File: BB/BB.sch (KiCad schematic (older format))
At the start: 14 parts, among them SW0 SW_Push, U1 AT90USB1286-AU, Y0 16Mhz

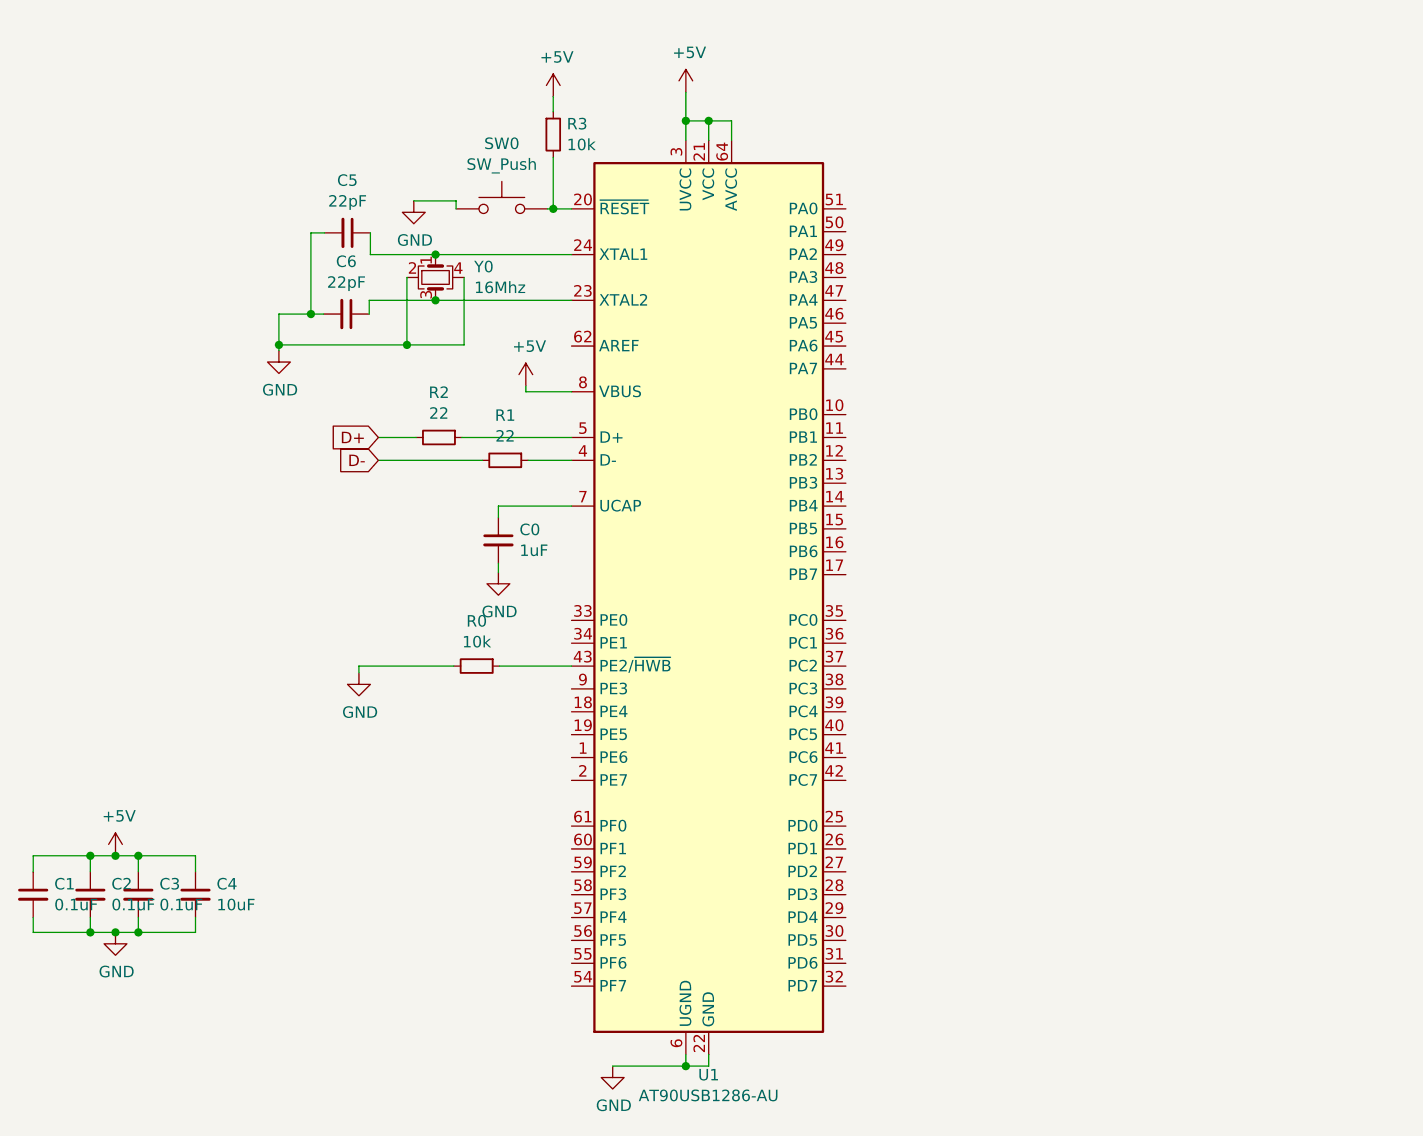
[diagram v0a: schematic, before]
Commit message: USB Molex
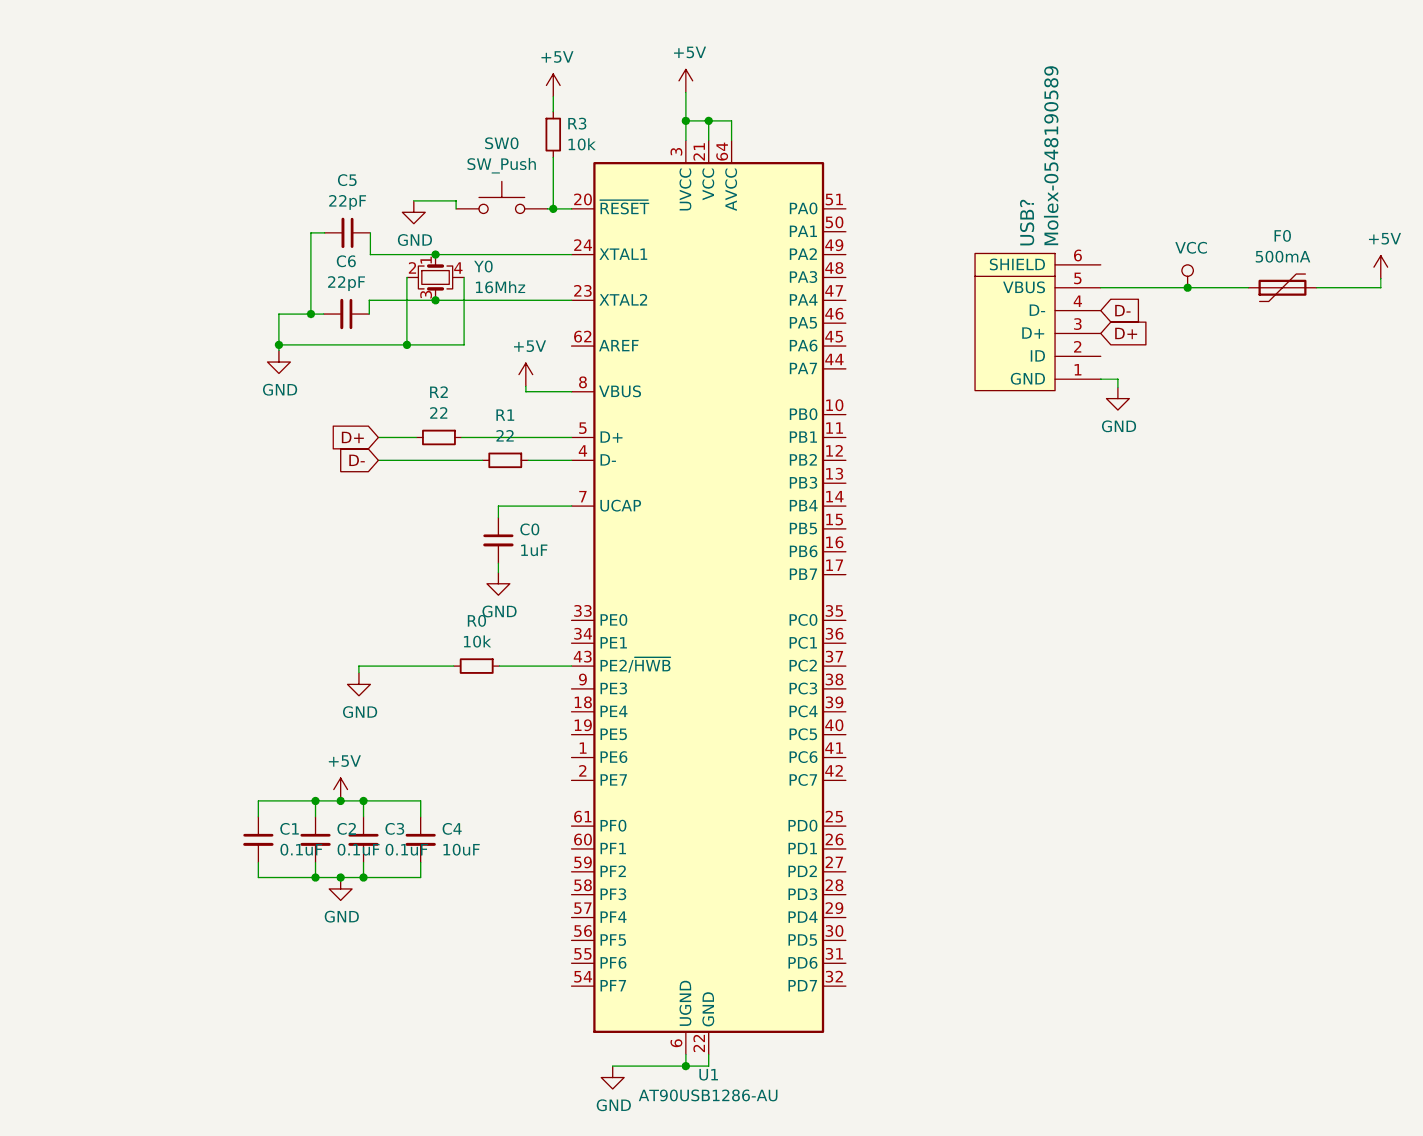
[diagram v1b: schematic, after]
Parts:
- added F0: 500mA, symbol Device:Polyfuse
- added USB?: Molex-0548190589, symbol random-keyboard-parts:Molex-0548190589
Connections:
- net +5V: now also F0.2
- net D+: now also USB?.3 (D+)
- net D-: now also USB?.4 (D-)
- net GND: now also USB?.1 (GND)
- new net VCC: F0.1, USB?.5 (VBUS)
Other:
- moved on the sheet: C1, C2, C3, C4
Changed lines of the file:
@@
 L Device:C_Small C2
 U 1 1 5CAFF9B8
-P 3100 4305
-F 0 "C2" H 3192 4351 50  0000 L CNN
-F 1 "0.1uF" H 3192 4260 50  0000 L CNN
-F 2 "" H 3100 4305 50  0001 C CNN
-F 3 "~" H 3100 4305 50  0001 C CNN
-	1    3100 4305
+P 4085 4065
+F 0 "C2" H 4177 4111 50  0000 L CNN
+F 1 "0.1uF" H 4177 4020 50  0000 L CNN
+F 2 "" H 4085 4065 50  0001 C CNN
+F 3 "~" H 4085 4065 50  0001 C CNN
+	1    4085 4065
 	1    0    0    -1
 $EndComp
@@
 L Device:C_Small C4
 U 1 1 5CB01275
-P 3560 4305
-F 0 "C4" H 3652 4351 50  0000 L CNN
-F 1 "10uF" H 3652 4260 50  0000 L CNN
-F 2 "" H 3560 4305 50  0001 C CNN
-F 3 "~" H 3560 4305 50  0001 C CNN
-	1    3560 4305
+P 4545 4065
+F 0 "C4" H 4637 4111 50  0000 L CNN
+F 1 "10uF" H 4637 4020 50  0000 L CNN
+F 2 "" H 4545 4065 50  0001 C CNN
+F 3 "~" H 4545 4065 50  0001 C CNN
+	1    4545 4065
 	1    0    0    -1
 $EndComp
@@
 L power:+5V #PWR?
 U 1 1 5CB01622
-P 3210 4135
-F 0 "#PWR?" H 3210 3985 50  0001 C CNN
-F 1 "+5V" H 3225 4308 50  0000 C CNN
-F 2 "" H 3210 4135 50  0001 C CNN
-F 3 "" H 3210 4135 50  0001 C CNN
-	1    3210 4135
+P 4195 3895
+F 0 "#PWR?" H 4195 3745 50  0001 C CNN
+F 1 "+5V" H 4210 4068 50  0000 C CNN
+F 2 "" H 4195 3895 50  0001 C CNN
+F 3 "" H 4195 3895 50  0001 C CNN
+	1    4195 3895
 	1    0    0    -1
 $EndComp
@@
 L power:GND #PWR?
 U 1 1 5CB02159
-P 3210 4470
-F 0 "#PWR?" H 3210 4220 50  0001 C CNN
-F 1 "GND" H 3215 4297 50  0000 C CNN
-F 2 "" H 3210 4470 50  0001 C CNN
-F 3 "" H 3210 4470 50  0001 C CNN
-	1    3210 4470
-	1    0    0    -1
-$EndComp
-Wire Wire Line
-	2850 4405 2850 4470
-Wire Wire Line
-	2850 4470 3100 4470
-Wire Wire Line
-	3210 4470 3310 4470
-Wire Wire Line
-	3560 4470 3560 4405
-Connection ~ 3210 4470
-Connection ~ 3310 4470
-Wire Wire Line
-	3310 4470 3560 4470
-Wire Wire Line
-	3100 4405 3100 4470
-Connection ~ 3100 4470
-Wire Wire Line
-	3100 4470 3210 4470
-Connection ~ 3210 4135
-Wire Wire Line
-	3310 4405 3310 4470
+P 4195 4230
+F 0 "#PWR?" H 4195 3980 50  0001 C CNN
+F 1 "GND" H 4200 4057 50  0000 C CNN
+F 2 "" H 4195 4230 50  0001 C CNN
+F 3 "" H 4195 4230 50  0001 C CNN
+	1    4195 4230
+	1    0    0    -1
+$EndComp
+Wire Wire Line
+	3835 4165 3835 4230
+Wire Wire Line
+	3835 4230 4085 4230
+Wire Wire Line
+	4195 4230 4295 4230
+Wire Wire Line
+	4545 4230 4545 4165
+Connection ~ 4195 4230
+Connection ~ 4295 4230
+Wire Wire Line
+	4295 4230 4545 4230
+Wire Wire Line
+	4085 4165 4085 4230
+Connection ~ 4085 4230
+Wire Wire Line
+	4085 4230 4195 4230
+Connection ~ 4195 3895
+Wire Wire Line
+	4295 4165 4295 4230
 $Comp
 L Device:C_Small C3
 U 1 1 5CB0126F
-P 3310 4305
-F 0 "C3" H 3402 4351 50  0000 L CNN
-F 1 "0.1uF" H 3402 4260 50  0000 L CNN
-F 2 "" H 3310 4305 50  0001 C CNN
-F 3 "~" H 3310 4305 50  0001 C CNN
-	1    3310 4305
+P 4295 4065
+F 0 "C3" H 4387 4111 50  0000 L CNN
+F 1 "0.1uF" H 4387 4020 50  0000 L CNN
+F 2 "" H 4295 4065 50  0001 C CNN
+F 3 "~" H 4295 4065 50  0001 C CNN
+	1    4295 4065
 	1    0    0    -1
 $EndComp
@@
 L Device:C_Small C1
 U 1 1 5CAFE031
-P 2850 4305
-F 0 "C1" H 2942 4351 50  0000 L CNN
-F 1 "0.1uF" H 2942 4260 50  0000 L CNN
-F 2 "" H 2850 4305 50  0001 C CNN
-F 3 "~" H 2850 4305 50  0001 C CNN
-	1    2850 4305
-	1    0    0    -1
-$EndComp
-Wire Wire Line
-	2850 4135 3100 4135
-Wire Wire Line
-	3210 4135 3310 4135
-Wire Wire Line
-	2850 4135 2850 4205
-Wire Wire Line
-	3100 4205 3100 4135
-Connection ~ 3100 4135
-Wire Wire Line
-	3100 4135 3210 4135
-Wire Wire Line
-	3310 4205 3310 4135
-Connection ~ 3310 4135
-Wire Wire Line
-	3310 4135 3560 4135
-Wire Wire Line
-	3560 4205 3560 4135
+P 3835 4065
+F 0 "C1" H 3927 4111 50  0000 L CNN
+F 1 "0.1uF" H 3927 4020 50  0000 L CNN
+F 2 "" H 3835 4065 50  0001 C CNN
+F 3 "~" H 3835 4065 50  0001 C CNN
+	1    3835 4065
+	1    0    0    -1
+$EndComp
+Wire Wire Line
+	3835 3895 4085 3895
+Wire Wire Line
+	4195 3895 4295 3895
+Wire Wire Line
+	3835 3895 3835 3965
+Wire Wire Line
+	4085 3965 4085 3895
+Connection ~ 4085 3895
+Wire Wire Line
+	4085 3895 4195 3895
+Wire Wire Line
+	4295 3965 4295 3895
+Connection ~ 4295 3895
+Wire Wire Line
+	4295 3895 4545 3895
+Wire Wire Line
+	4545 3965 4545 3895
 $Comp
 L power:+5V #PWR?
@@
 Text GLabel 4360 2405 0    50   Input ~ 0
 D-
+$Comp
+L random-keyboard-parts:Molex-0548190589 USB?
+U 1 1 5CB3B096
+P 7220 1850
+F 0 "USB?" H 7598 1870 60  0000 L CNN
+F 1 "Molex-0548190589" H 7598 1764 60  0000 L CNN
+F 2 "" H 7220 1850 60  0001 C CNN
+F 3 "" H 7220 1850 60  0001 C CNN
+	1    7220 1850
+	0    -1   -1   0
+$EndComp
+Text GLabel 7520 1850 2    50   Input ~ 0
+D+
+Text GLabel 7520 1750 2    50   Input ~ 0
+D-
+$Comp
+L power:VCC #PWR?
+U 1 1 5CB3D7F1
+P 7900 1650
+F 0 "#PWR?" H 7900 1500 50  0001 C CNN
+F 1 "VCC" H 7917 1823 50  0000 C CNN
+F 2 "" H 7900 1650 50  0001 C CNN
+F 3 "" H 7900 1650 50  0001 C CNN
+	1    7900 1650
+	1    0    0    -1
+$EndComp
+$Comp
+L Device:Polyfuse F0
+U 1 1 5CB3FDE1
+P 8315 1650
+F 0 "F0" V 8540 1650 50  0000 C CNN
+F 1 "500mA" V 8449 1650 50  0000 C CNN
+F 2 "" H 8365 1450 50  0001 L CNN
+F 3 "~" H 8315 1650 50  0001 C CNN
+	1    8315 1650
+	0    -1   -1   0
+$EndComp
+Wire Wire Line
+	7520 1650 7900 1650
+Wire Wire Line
+	7900 1650 8165 1650
+Connection ~ 7900 1650
+$Comp
+L power:+5V #PWR?
+U 1 1 5CB43D86
+P 8745 1610
+F 0 "#PWR?" H 8745 1460 50  0001 C CNN
+F 1 "+5V" H 8760 1783 50  0000 C CNN
+F 2 "" H 8745 1610 50  0001 C CNN
+F 3 "" H 8745 1610 50  0001 C CNN
+	1    8745 1610
+	1    0    0    -1
+$EndComp
+Wire Wire Line
+	8465 1650 8745 1650
+Wire Wire Line
+	8745 1650 8745 1610
+$Comp
+L power:GND #PWR?
+U 1 1 5CB48029
+P 7595 2085
+F 0 "#PWR?" H 7595 1835 50  0001 C CNN
+F 1 "GND" H 7600 1912 50  0000 C CNN
+F 2 "" H 7595 2085 50  0001 C CNN
+F 3 "" H 7595 2085 50  0001 C CNN
+	1    7595 2085
+	1    0    0    -1
+$EndComp
+Wire Wire Line
+	7520 2050 7595 2050
+Wire Wire Line
+	7595 2050 7595 2085
 $EndSCHEMATC

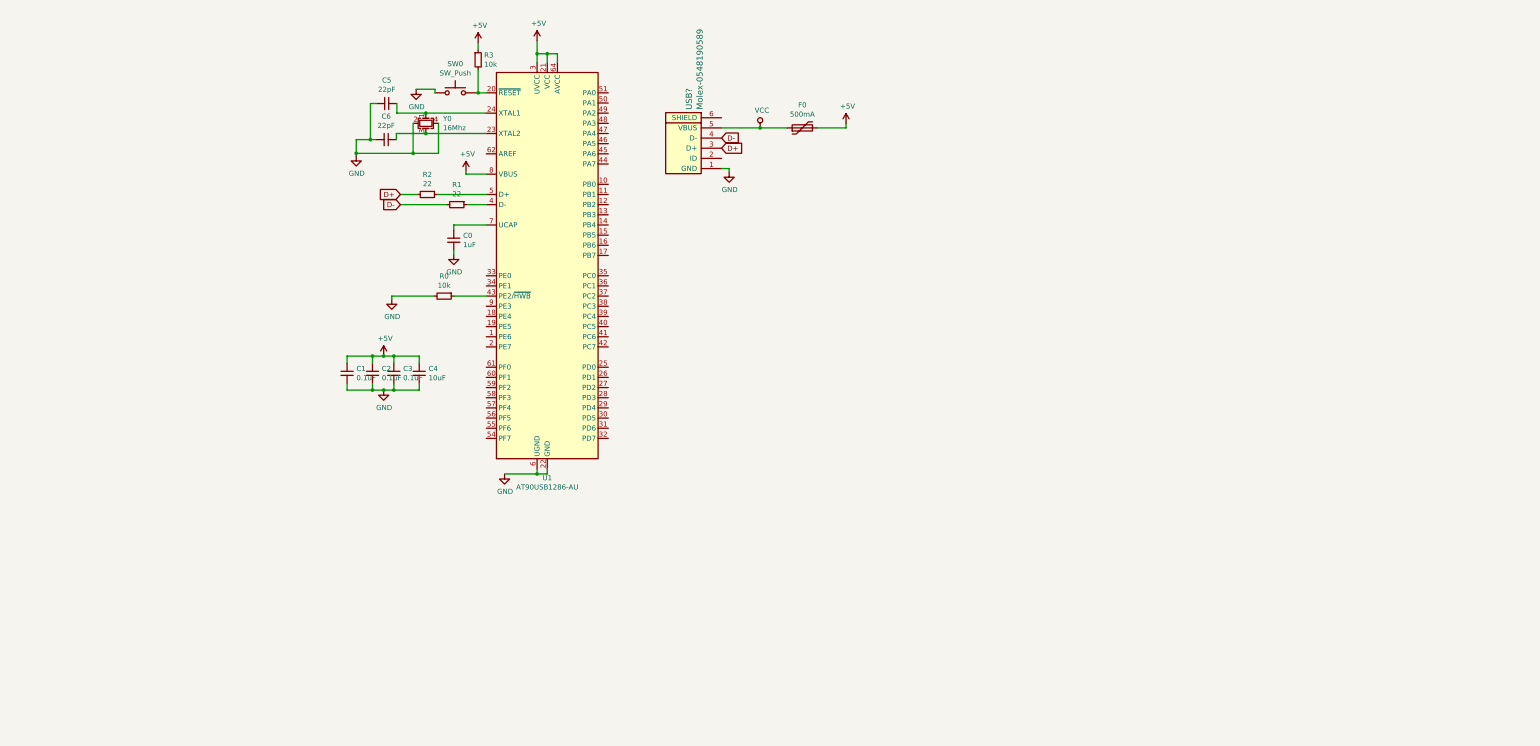
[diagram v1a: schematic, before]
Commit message: Numpad Switches Added
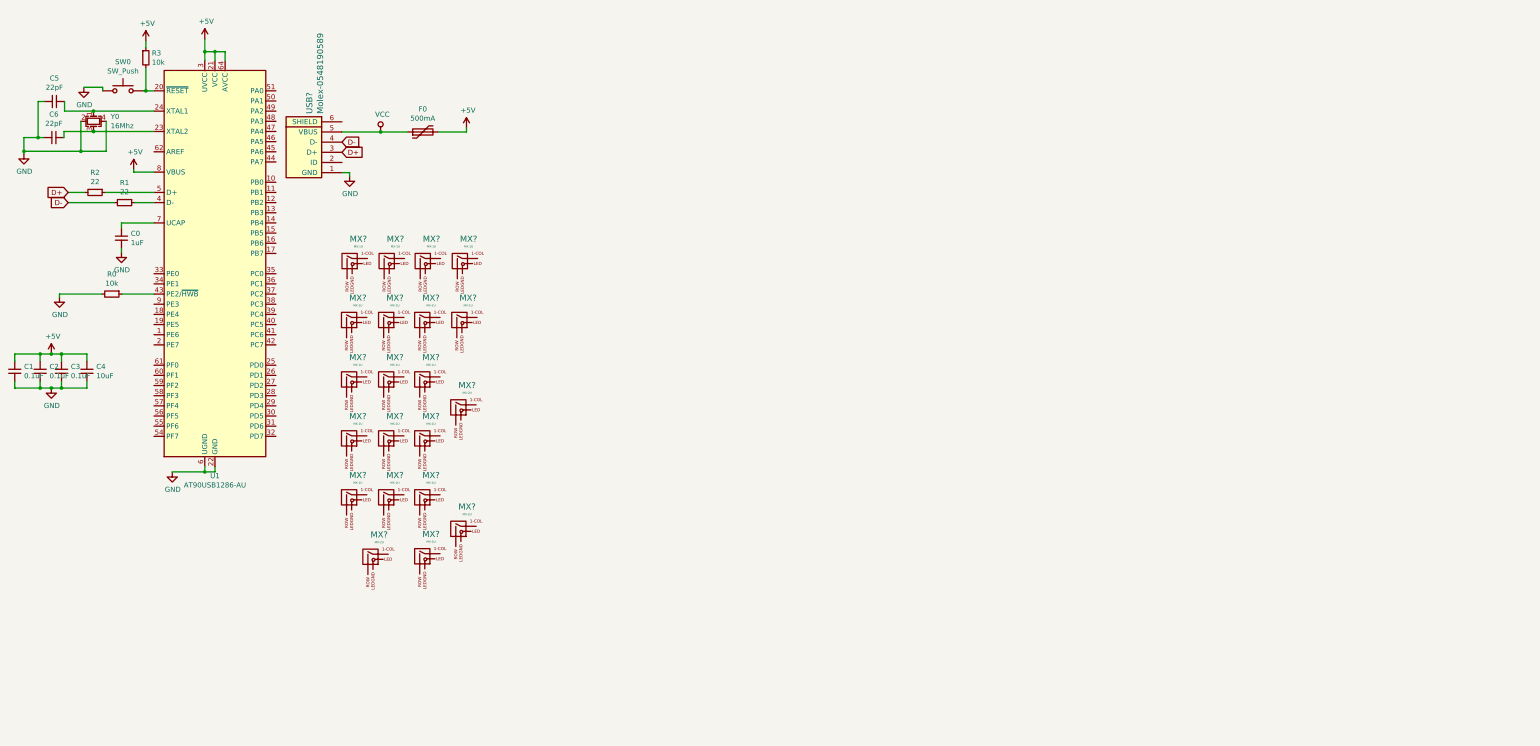
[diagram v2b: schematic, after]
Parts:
- added MX? (x18): MX-1U, symbol MX_Alps_Hybrids:MX-1U
- added MX? (x3): MX-2U, symbol MX_Alps_Hybrids:MX-2U
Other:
- moved on the sheet: C0, C1, C2, C3, C4, C5, C6, F0, R0, R1, R2, R3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
